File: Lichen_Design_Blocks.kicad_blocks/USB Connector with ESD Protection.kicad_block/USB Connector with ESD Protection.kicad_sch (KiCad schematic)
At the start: 4 parts, among them J2 USB_C_Receptacle_USB2.0_16P, U3 USBLC6-2SC6

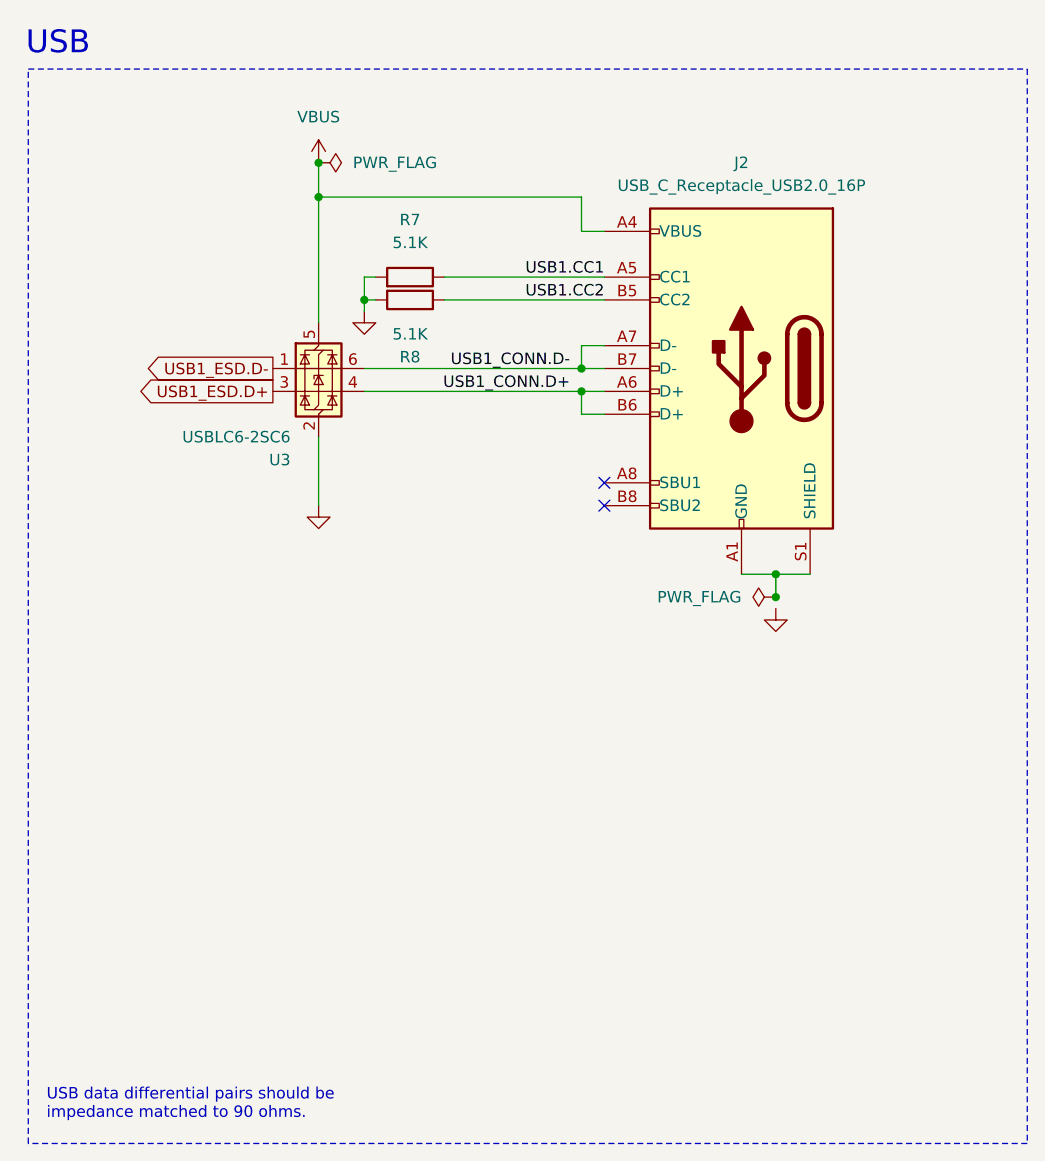
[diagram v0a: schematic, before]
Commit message: feat: Updates symbol libraries and design blocks. Adds in-progress RP2350-based module.
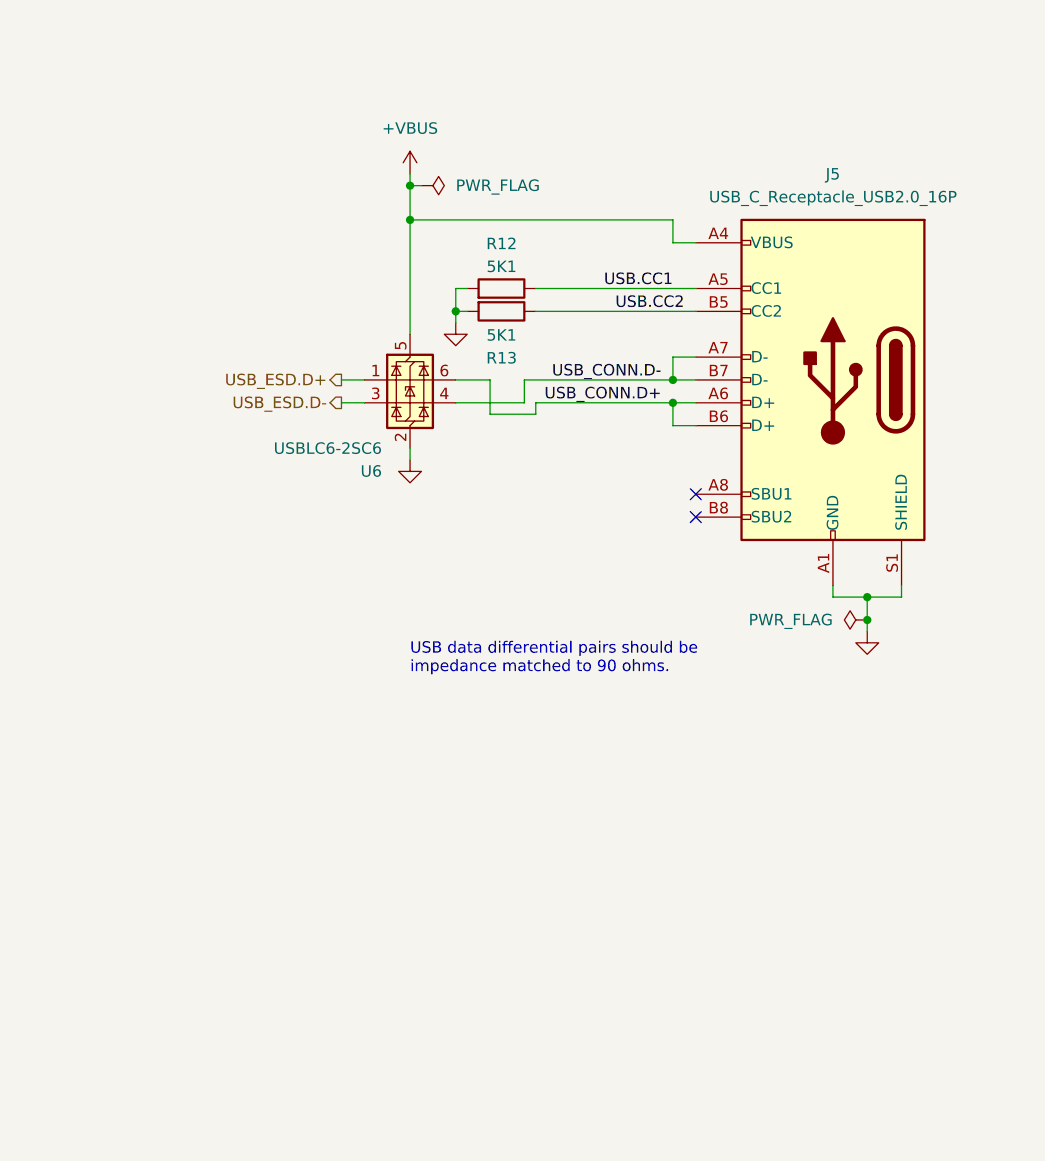
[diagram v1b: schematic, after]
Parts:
- R12: renamed from R7; value 5k1_0603 -> 5.1K; Display 5.1K -> 5K1
- R13: renamed from R8; value 5k1_0603 -> 5.1K; Display 5.1K -> 5K1
- renumbered J2 to J5, U3 to U6
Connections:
- net GND: now also J5.A1 (GND), J5.A12 (GND), J5.B1 (GND), J5.B12 (GND), J5.S1 (SHIELD)
- net USB1.CC1 renamed USB.CC1
- net USB1.CC2 renamed USB.CC2
- net USB1_CONN.D+ renamed USB_CONN.D+
- net USB_CONN.D+: now also U6.6 (I/O1); no longer U6.4 (I/O2)
- net USB1_CONN.D- renamed USB_CONN.D-
- net USB_CONN.D-: now also U6.4 (I/O2); no longer U6.6 (I/O1)
- net USB1_ESD.D+ renamed USB_ESD.D-
- net USB1_ESD.D- renamed USB_ESD.D+
- net VBUS renamed +VBUS
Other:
- note removed: "USB"
- moved on the sheet: J5, R12, R13, U6
